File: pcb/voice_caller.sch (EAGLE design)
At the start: 36 parts, among them IC1 PRO_MICRO, IC2 AT45DB321D-S, IC3 78L12SMD, K1 TQ2SA-L2-5V

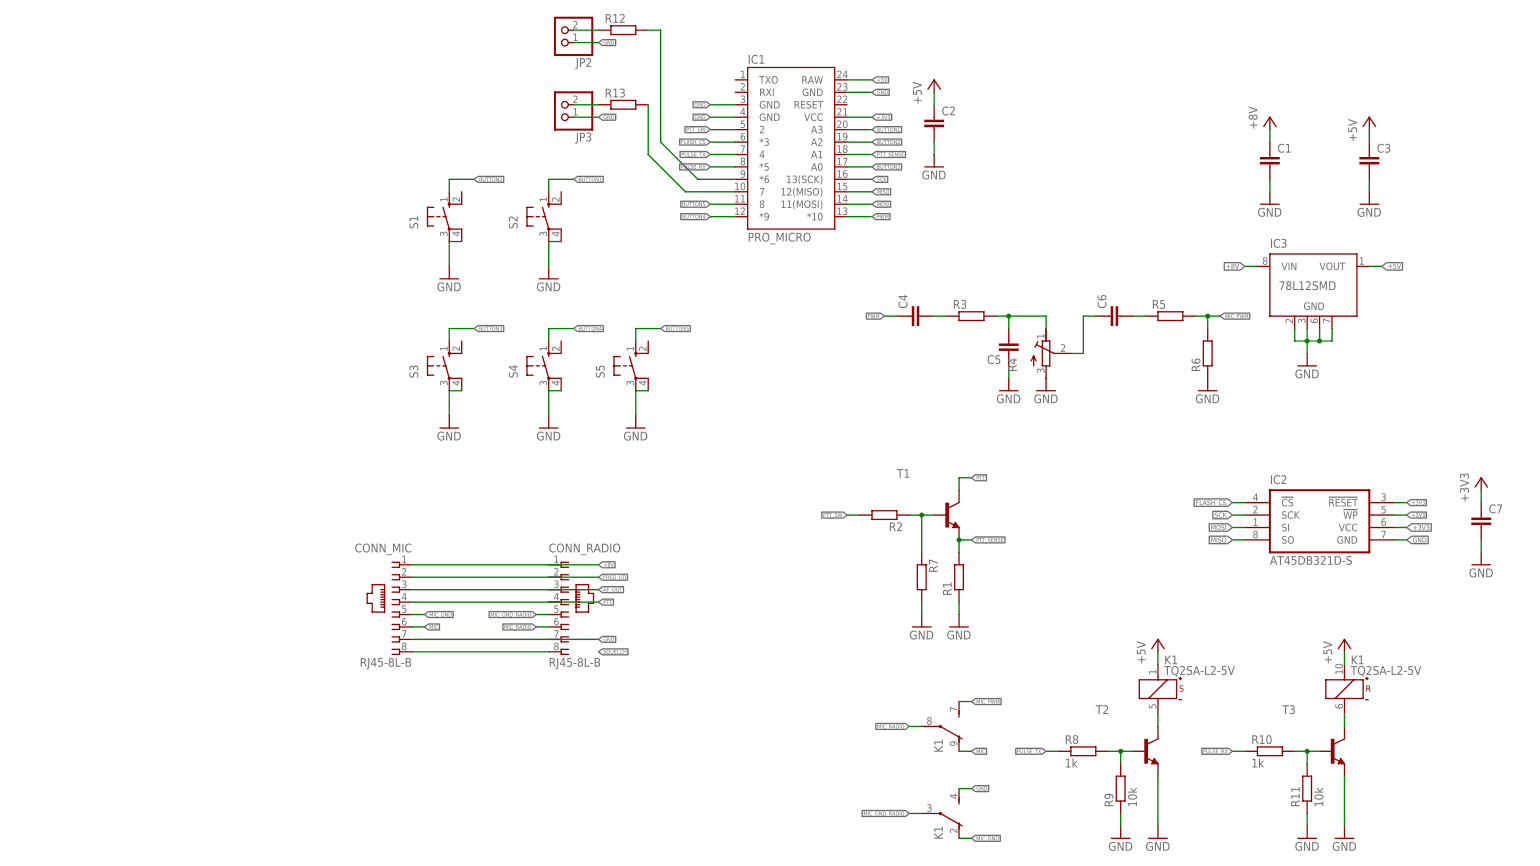
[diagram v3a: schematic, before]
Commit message: RC values added.
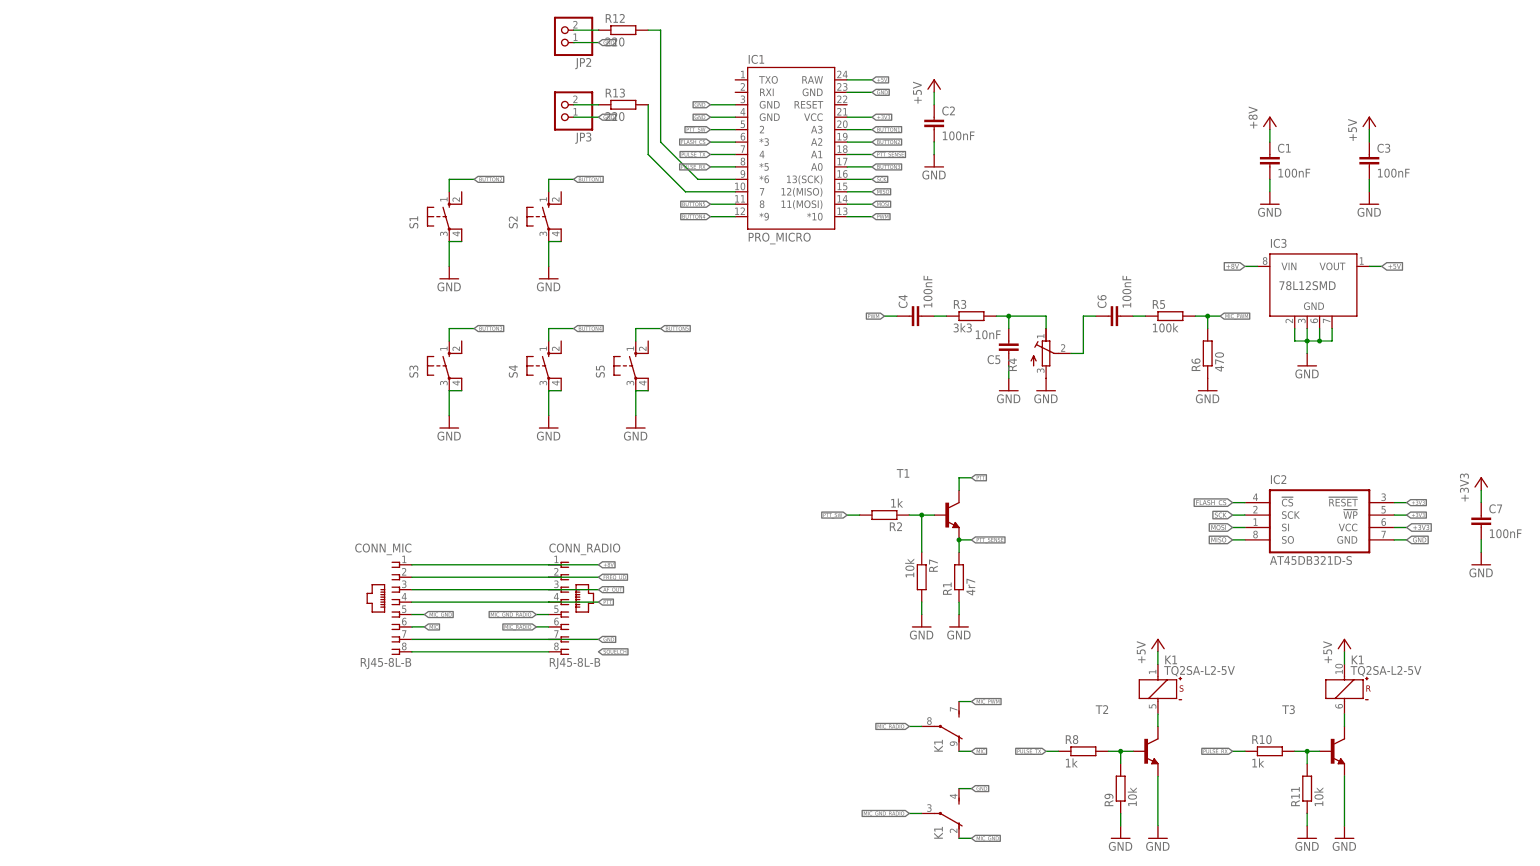
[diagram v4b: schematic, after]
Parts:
- C1, C2, C3, C4, C6, C7: value (none) -> 100nF
- C5: value (none) -> 10nF
- R1: value (none) -> 4r7
- R12, R13: value (none) -> 220
- R2: value (none) -> 1k
- R3: value (none) -> 3k3
- R5: value (none) -> 100k
- R6: value (none) -> 470
- R7: value (none) -> 10k
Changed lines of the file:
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@@
 <part name="P+2" library="supply1" deviceset="+5V" device=""/>
 <part name="GND2" library="supply1" deviceset="GND" device=""/>
-<part name="C1" library="rcl" deviceset="C-EU" device="C1206K"/>
-<part name="C2" library="rcl" deviceset="C-EU" device="C1206K"/>
+<part name="C1" library="rcl" deviceset="C-EU" device="C1206K" value="100nF"/>
+<part name="C2" library="rcl" deviceset="C-EU" device="C1206K" value="100nF"/>
 <part name="IC2" library="memory-atmel" deviceset="AT45DB321D-S" device=""/>
-<part name="C3" library="rcl" deviceset="C-EU" device="C1206K"/>
+<part name="C3" library="rcl" deviceset="C-EU" device="C1206K" value="100nF"/>
 <part name="P+1" library="supply1" deviceset="+5V" device=""/>
 <part name="GND3" library="supply1" deviceset="GND" device=""/>
@@
 <part name="GND5" library="supply1" deviceset="GND" device=""/>
 <part name="GND6" library="supply1" deviceset="GND" device=""/>
-<part name="C4" library="rcl" deviceset="C-EU" device="C1206K"/>
-<part name="R3" library="rcl" deviceset="R-EU_" device="M1206"/>
-<part name="C5" library="rcl" deviceset="C-EU" device="C1206K"/>
+<part name="C4" library="rcl" deviceset="C-EU" device="C1206K" value="100nF"/>
+<part name="R3" library="rcl" deviceset="R-EU_" device="M1206" value="3k3"/>
+<part name="C5" library="rcl" deviceset="C-EU" device="C1206K" value="10nF"/>
 <part name="GND7" library="supply1" deviceset="GND" device=""/>
 <part name="R4" library="rcl" deviceset="R-TRIMM" device="T93XB"/>
 <part name="GND8" library="supply1" deviceset="GND" device=""/>
-<part name="C6" library="rcl" deviceset="C-EU" device="C1206K"/>
-<part name="R5" library="rcl" deviceset="R-EU_" device="M1206"/>
-<part name="R6" library="rcl" deviceset="R-EU_" device="M1206"/>
+<part name="C6" library="rcl" deviceset="C-EU" device="C1206K" value="100nF"/>
+<part name="R5" library="rcl" deviceset="R-EU_" device="M1206" value="100k"/>
+<part name="R6" library="rcl" deviceset="R-EU_" device="M1206" value="470"/>
 <part name="GND9" library="supply1" deviceset="GND" device=""/>
-<part name="C7" library="rcl" deviceset="C-EU" device="C1206K"/>
+<part name="C7" library="rcl" deviceset="C-EU" device="C1206K" value="100nF"/>
 <part name="GND11" library="supply1" deviceset="GND" device=""/>
 <part name="+3V1" library="supply1" deviceset="+3V3" device=""/>
@@
 <part name="GND17" library="supply1" deviceset="GND" device=""/>
 <part name="T1" library="transistor" deviceset="*-NPN-" device="SOT23-BEC" technology="MMBT3904LT1"/>
-<part name="R1" library="rcl" deviceset="R-EU_" device="M1206"/>
+<part name="R1" library="rcl" deviceset="R-EU_" device="M1206" value="4r7"/>
 <part name="GND18" library="supply1" deviceset="GND" device=""/>
-<part name="R2" library="rcl" deviceset="R-EU_" device="M1206"/>
-<part name="R7" library="rcl" deviceset="R-EU_" device="M1206"/>
+<part name="R2" library="rcl" deviceset="R-EU_" device="M1206" value="1k"/>
+<part name="R7" library="rcl" deviceset="R-EU_" device="M1206" value="10k"/>
 <part name="GND19" library="supply1" deviceset="GND" device=""/>
-<part name="R12" library="rcl" deviceset="R-EU_" device="M1206"/>
-<part name="R13" library="rcl" deviceset="R-EU_" device="M1206"/>
+<part name="R12" library="rcl" deviceset="R-EU_" device="M1206" value="220"/>
+<part name="R13" library="rcl" deviceset="R-EU_" device="M1206" value="220"/>
 <part name="JP2" library="pinhead" deviceset="PINHD-1X2" device=""/>
 <part name="JP3" library="pinhead" deviceset="PINHD-1X2" device=""/>

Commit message: Values adjusted.
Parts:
- C4: value 100nF -> 100uF
- R5: value 100k -> 4k7
- R6: value 470 -> NP
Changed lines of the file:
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@@
 <part name="GND5" library="supply1" deviceset="GND" device=""/>
 <part name="GND6" library="supply1" deviceset="GND" device=""/>
-<part name="C4" library="rcl" deviceset="C-EU" device="C1206K" value="100nF"/>
+<part name="C4" library="rcl" deviceset="C-EU" device="C1206K" value="100uF"/>
 <part name="R3" library="rcl" deviceset="R-EU_" device="M1206" value="3k3"/>
 <part name="C5" library="rcl" deviceset="C-EU" device="C1206K" value="10nF"/>
@@
 <part name="GND8" library="supply1" deviceset="GND" device=""/>
 <part name="C6" library="rcl" deviceset="C-EU" device="C1206K" value="100nF"/>
-<part name="R5" library="rcl" deviceset="R-EU_" device="M1206" value="100k"/>
-<part name="R6" library="rcl" deviceset="R-EU_" device="M1206" value="470"/>
+<part name="R5" library="rcl" deviceset="R-EU_" device="M1206" value="4k7"/>
+<part name="R6" library="rcl" deviceset="R-EU_" device="M1206" value="NP"/>
 <part name="GND9" library="supply1" deviceset="GND" device=""/>
 <part name="C7" library="rcl" deviceset="C-EU" device="C1206K" value="100nF"/>

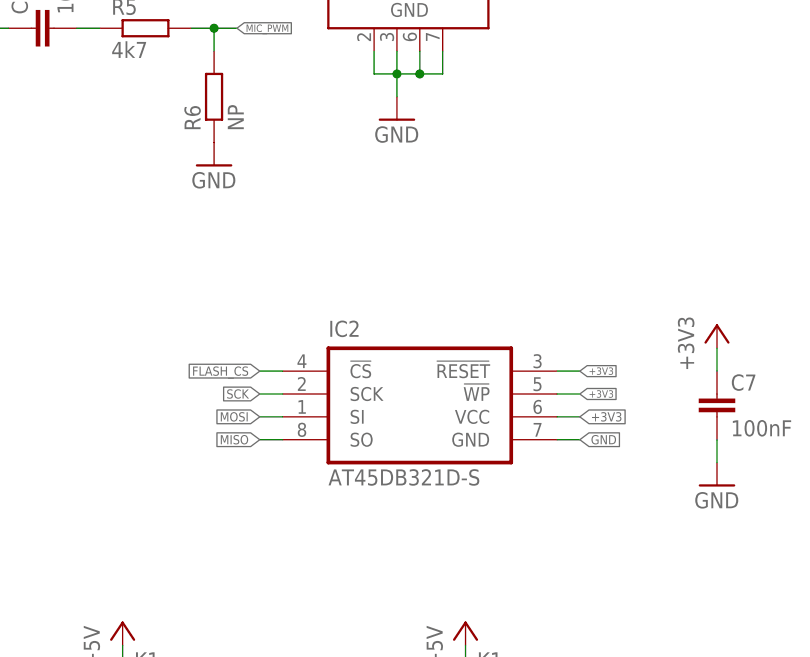
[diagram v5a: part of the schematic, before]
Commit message: Flash IC replaced and almost routed.
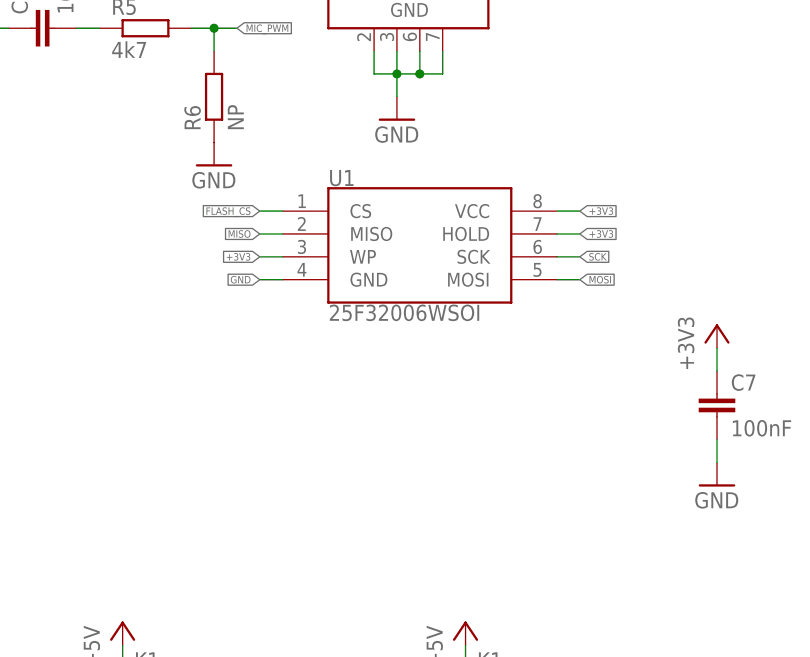
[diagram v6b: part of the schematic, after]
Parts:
- removed IC2: AT45DB321D-S, memory-atmel:AT45DB321D-S
- added U1: 25F32006WSOI, SparkFun-IC-Memory:SPI_FLASH-X25XXSMD1
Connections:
- net +3V3: now also U1.HOLD, U1.VCC, U1.WP; no longer IC2.!RESET!, IC2.!WP!, IC2.VCC
- net FLASH_CS: now also U1.CS; no longer IC2.!CS!
- net GND: now also U1.GND; no longer IC2.GND
- net MISO: now also U1.MISO; no longer IC2.SO
- net MOSI: now also U1.MOSI; no longer IC2.SI
- net SCK: now also U1.SCK; no longer IC2.SCK
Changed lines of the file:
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@@
 <part name="C1" library="rcl" deviceset="C-EU" device="C1206K" value="100nF"/>
 <part name="C2" library="rcl" deviceset="C-EU" device="C1206K" value="100nF"/>
-<part name="IC2" library="memory-atmel" deviceset="AT45DB321D-S" device=""/>
 <part name="C3" library="rcl" deviceset="C-EU" device="C1206K" value="100nF"/>
 <part name="P+1" library="supply1" deviceset="+5V" device=""/>
@@
 <part name="JP2" library="pinhead" deviceset="PINHD-1X2" device=""/>
 <part name="JP3" library="pinhead" deviceset="PINHD-1X2" device=""/>
+<part name="U1" library="SparkFun-IC-Memory" deviceset="SPI_FLASH-X25XX" device="SMD1" value="25F32006WSOI"/>
 </parts>
 <sheets>
@@
 <instance part="C1" gate="G$1" x="147.32" y="142.24"/>
 <instance part="C2" gate="G$1" x="78.74" y="149.86"/>
-<instance part="IC2" gate="G$1" x="157.48" y="68.58"/>
 <instance part="C3" gate="G$1" x="167.64" y="142.24"/>
 <instance part="P+1" gate="1" x="167.64" y="149.86"/>
@@
 <instance part="JP2" gate="G$1" x="2.54" y="167.64" rot="R180"/>
 <instance part="JP3" gate="G$1" x="2.54" y="152.4" rot="R180"/>
+<instance part="U1" gate="G$1" x="157.48" y="86.36"/>
 </instances>
 <busses>
@@
 <pinref part="C2" gate="G$1" pin="2"/>
 <wire x1="78.74" y1="142.24" x2="78.74" y2="144.78" width="0.1524" layer="91"/>
-</segment>
-<segment>
-<pinref part="IC2" gate="G$1" pin="GND"/>
-<wire x1="172.72" y1="63.5" x2="175.26" y2="63.5" width="0.1524" layer="91"/>
-<label x="175.26" y="63.5" size="1.016" layer="95" xref="yes"/>
 </segment>
 <segment>
@@
 <pinref part="JP3" gate="G$1" pin="1"/>
 </segment>
+<segment>
+<pinref part="U1" gate="G$1" pin="GND"/>
+<wire x1="142.24" y1="81.28" x2="139.7" y2="81.28" width="0.1524" layer="91"/>
+<label x="139.7" y="81.28" size="0.8128" layer="95" rot="R180" xref="yes"/>
+</segment>
 </net>
 <net name="MOSI" class="0">
-<segment>
-<pinref part="IC2" gate="G$1" pin="SI"/>
-<wire x1="142.24" y1="66.04" x2="139.7" y2="66.04" width="0.1524" layer="91"/>
-<label x="139.7" y="66.04" size="1.016" layer="95" rot="R180" xref="yes"/>
-</segment>
 <segment>
 <pinref part="IC1" gate="G$1" pin="11(MOSI)"/>
@@
 <label x="66.04" y="132.08" size="0.8128" layer="95" xref="yes"/>
 </segment>
+<segment>
+<pinref part="U1" gate="G$1" pin="MOSI"/>
+<wire x1="172.72" y1="81.28" x2="175.26" y2="81.28" width="0.1524" layer="91"/>
+<label x="175.26" y="81.28" size="0.8128" layer="95" xref="yes"/>
+</segment>
 </net>
 <net name="MISO" class="0">
-<segment>
-<pinref part="IC2" gate="G$1" pin="SO"/>
-<wire x1="142.24" y1="63.5" x2="139.7" y2="63.5" width="0.1524" layer="91"/>
-<label x="139.7" y="63.5" size="1.016" layer="95" rot="R180" xref="yes"/>
-</segment>
 <segment>
 <pinref part="IC1" gate="G$1" pin="12(MISO)"/>
@@
 <label x="66.04" y="134.62" size="0.8128" layer="95" xref="yes"/>
 </segment>
+<segment>
+<pinref part="U1" gate="G$1" pin="MISO"/>
+<wire x1="142.24" y1="86.36" x2="139.7" y2="86.36" width="0.1524" layer="91"/>
+<label x="139.7" y="86.36" size="0.8128" layer="95" rot="R180" xref="yes"/>
+</segment>
 </net>
 <net name="SCK" class="0">
-<segment>
-<pinref part="IC2" gate="G$1" pin="SCK"/>
-<wire x1="142.24" y1="68.58" x2="139.7" y2="68.58" width="0.1524" layer="91"/>
-<label x="139.7" y="68.58" size="1.016" layer="95" rot="R180" xref="yes"/>
-</segment>
 <segment>
 <pinref part="IC1" gate="G$1" pin="13(SCK)"/>
@@
 <label x="66.04" y="137.16" size="0.8128" layer="95" xref="yes"/>
 </segment>
+<segment>
+<pinref part="U1" gate="G$1" pin="SCK"/>
+<wire x1="172.72" y1="83.82" x2="175.26" y2="83.82" width="0.1524" layer="91"/>
+<label x="175.26" y="83.82" size="0.8128" layer="95" xref="yes"/>
+</segment>
 </net>
 <net name="FLASH_CS" class="0">
-<segment>
-<pinref part="IC2" gate="G$1" pin="!CS!"/>
-<wire x1="142.24" y1="71.12" x2="139.7" y2="71.12" width="0.1524" layer="91"/>
-<label x="139.7" y="71.12" size="1.016" layer="95" rot="R180" xref="yes"/>
-</segment>
 <segment>
 <pinref part="IC1" gate="G$1" pin="*3"/>
 <wire x1="38.1" y1="144.78" x2="33.02" y2="144.78" width="0.1524" layer="91"/>
 <label x="33.02" y="144.78" size="0.8128" layer="95" rot="R180" xref="yes"/>
+</segment>
+<segment>
+<pinref part="U1" gate="G$1" pin="CS"/>
+<wire x1="142.24" y1="88.9" x2="139.7" y2="88.9" width="0.1524" layer="91"/>
+<label x="139.7" y="88.9" size="0.8128" layer="95" rot="R180" xref="yes"/>
 </segment>
 </net>
@@
 </segment>
 <segment>
-<pinref part="IC2" gate="G$1" pin="VCC"/>
-<wire x1="172.72" y1="66.04" x2="175.26" y2="66.04" width="0.1524" layer="91"/>
-<label x="175.26" y="66.04" size="1.016" layer="95" xref="yes"/>
-</segment>
-<segment>
 <pinref part="C7" gate="G$1" pin="1"/>
 <wire x1="190.5" y1="71.12" x2="190.5" y2="73.66" width="0.1524" layer="91"/>
@@
 </segment>
 <segment>
-<pinref part="IC2" gate="G$1" pin="!RESET!"/>
-<wire x1="172.72" y1="71.12" x2="175.26" y2="71.12" width="0.1524" layer="91"/>
-<label x="175.26" y="71.12" size="0.8128" layer="95" xref="yes"/>
-</segment>
-<segment>
-<pinref part="IC2" gate="G$1" pin="!WP!"/>
-<wire x1="172.72" y1="68.58" x2="175.26" y2="68.58" width="0.1524" layer="91"/>
-<label x="175.26" y="68.58" size="0.8128" layer="95" xref="yes"/>
-</segment>
-</net>
+<pinref part="U1" gate="G$1" pin="WP"/>
+<wire x1="142.24" y1="83.82" x2="139.7" y2="83.82" width="0.1524" layer="91"/>
+<label x="139.7" y="83.82" size="0.8128" layer="95" rot="R180" xref="yes"/>
+</segment>
+<segment>
+<pinref part="U1" gate="G$1" pin="HOLD"/>
+<wire x1="172.72" y1="86.36" x2="175.26" y2="86.36" width="0.1524" layer="91"/>
+<label x="175.26" y="86.36" size="0.8128" layer="95" xref="yes"/>
+</segment>
+<segment>
+<pinref part="U1" gate="G$1" pin="VCC"/>
+<wire x1="172.72" y1="88.9" x2="175.26" y2="88.9" width="0.1524" layer="91"/>
+<label x="175.26" y="88.9" size="0.8128" layer="95" xref="yes"/>
+</segment>
+</net>
